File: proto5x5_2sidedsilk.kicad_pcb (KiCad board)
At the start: 2 copper layers, 50 x 50 mm, 5 parts

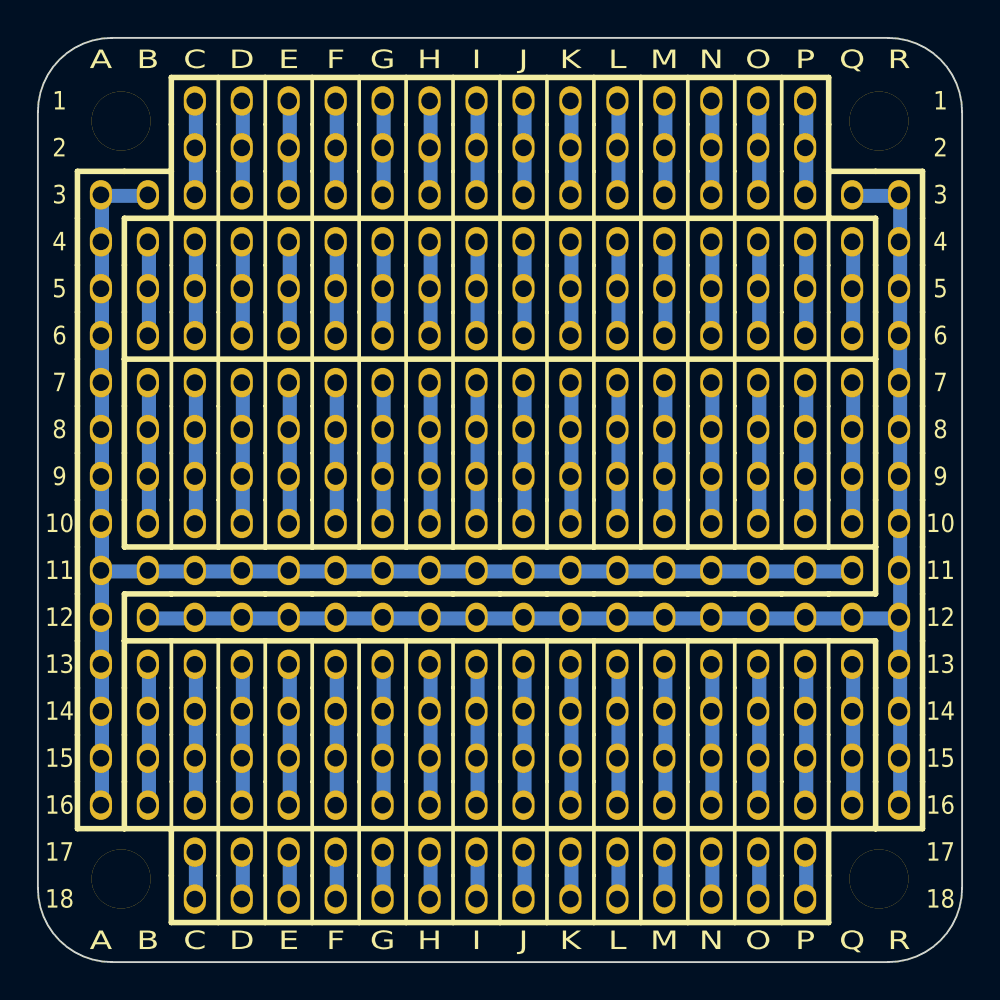
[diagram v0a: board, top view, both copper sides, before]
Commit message: Add improved pads (large horizontal/vertical) and rocket logo.
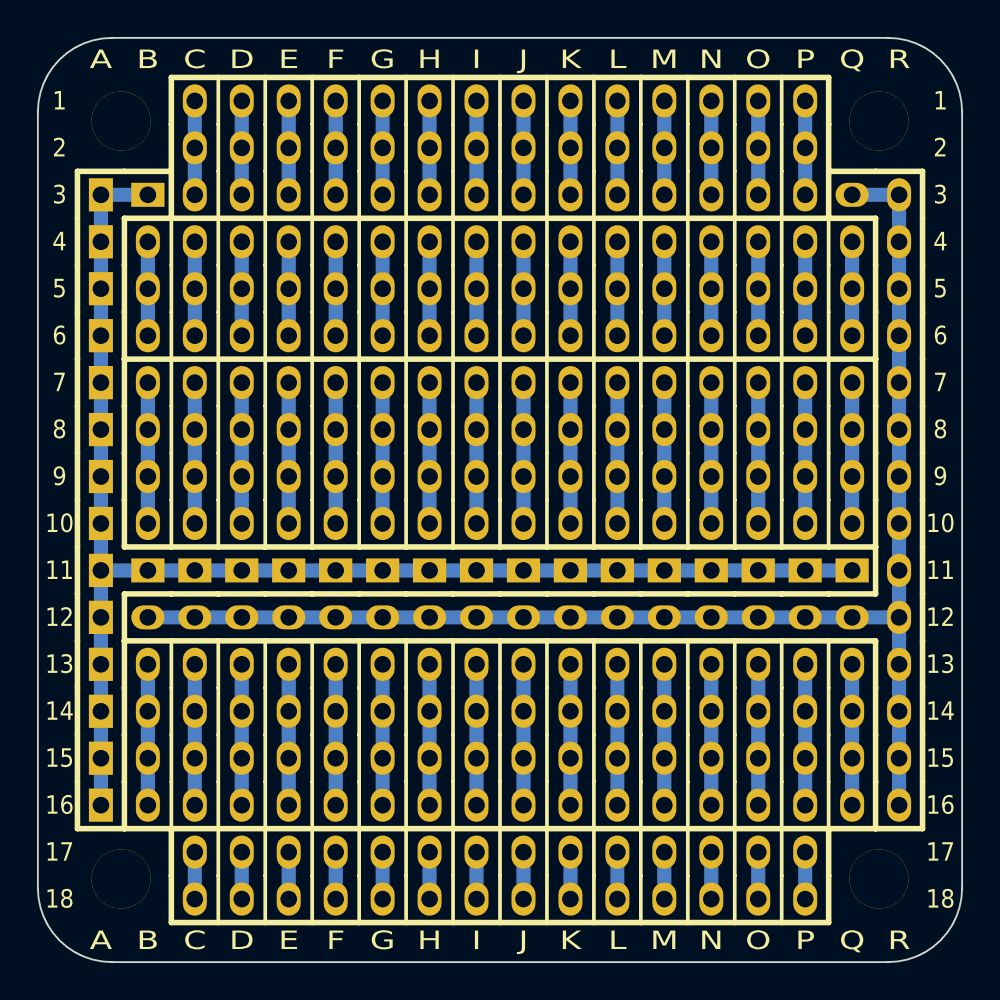
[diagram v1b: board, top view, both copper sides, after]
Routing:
- net VCC1: track 81.0 -> 76.2 mm
- net GND: track 81.0 -> 76.2 mm
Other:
- net class Default removed
- rule trace_clearance: 0.254 -> 0.762
